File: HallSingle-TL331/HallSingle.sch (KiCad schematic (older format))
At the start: 11 parts, among them J1 Conn_01x03, U1 SS49E, U2 TL331

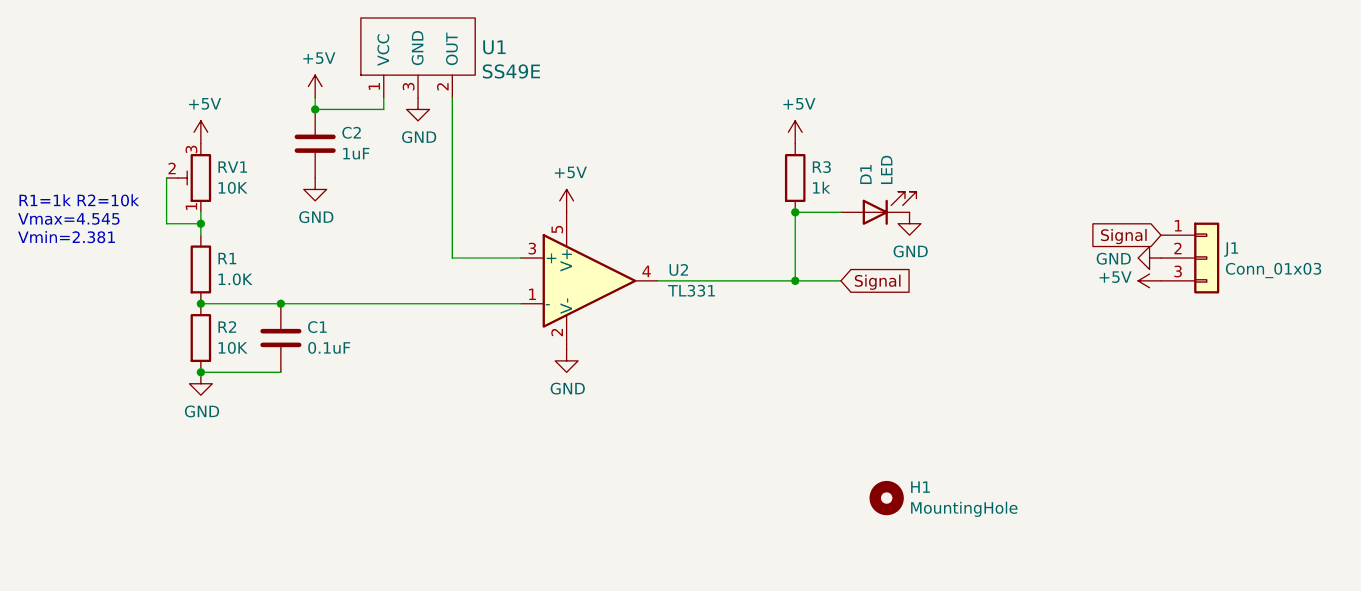
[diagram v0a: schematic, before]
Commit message: Fixed TL orientation. ( previously fixed an error that was not an error ) thining is hard sometimes.
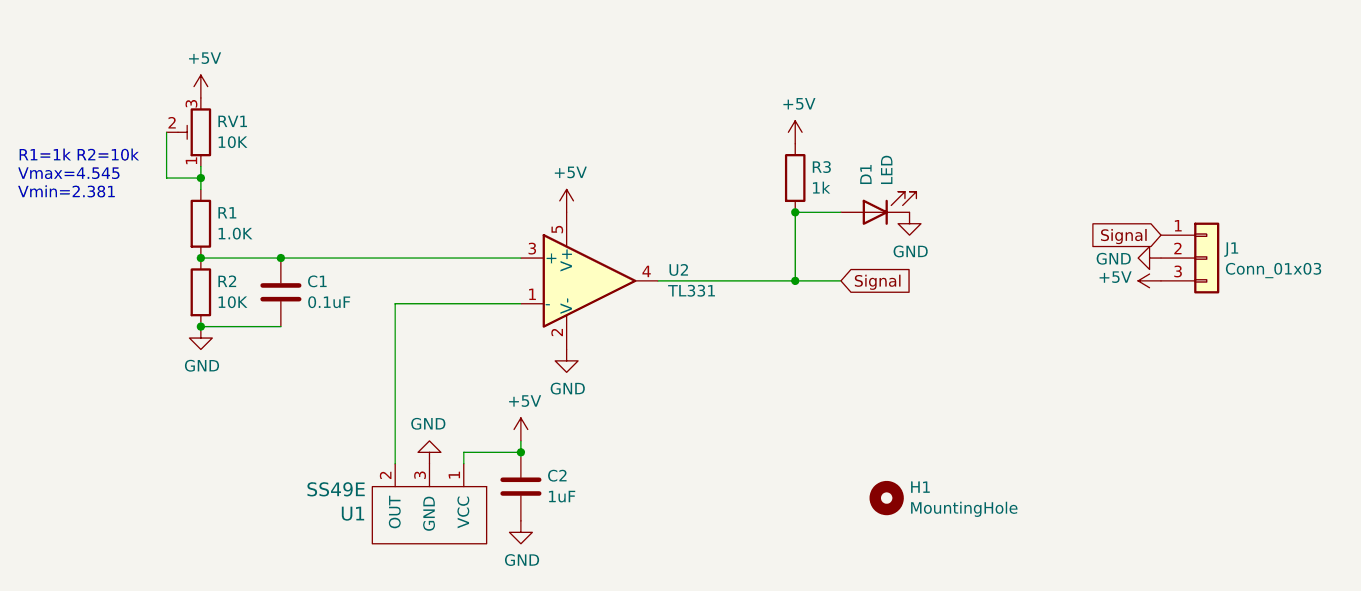
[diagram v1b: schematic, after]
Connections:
- net at U1.2 (OUT): now also U2.1 (-); no longer U2.3 (+)
- net at C1.1, R1.2, R2.1: now also U2.3 (+); no longer U2.1 (-)
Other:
- moved on the sheet: C1, C2, R1, R2, RV1, U1
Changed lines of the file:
@@
 L HallEffect:SS49E U1
 U 1 1 5FEA3EB5
-P 4050 1500
-F 0 "U1" H 4328 1620 60  0000 L CNN
-F 1 "SS49E" H 4328 1514 60  0000 L CNN
-F 2 "HallEffect:SOT-23" H 3950 1500 60  0001 C CNN
-F 3 "" H 3950 1500 60  0001 C CNN
-	1    4050 1500
-	1    0    0    -1
+P 4100 3300
+F 0 "U1" H 4378 3420 60  0000 L CNN
+F 1 "SS49E" H 4378 3314 60  0000 L CNN
+F 2 "HallEffect:SOT-23" H 4000 3300 60  0001 C CNN
+F 3 "" H 4000 3300 60  0001 C CNN
+	1    4100 3300
+	-1   0    0    1
 $EndComp
 $Comp
 L power:GND #PWR05
 U 1 1 5FEA483D
-P 4050 1600
-F 0 "#PWR05" H 4050 1350 50  0001 C CNN
-F 1 "GND" H 4055 1427 50  0000 C CNN
-F 2 "" H 4050 1600 50  0001 C CNN
-F 3 "" H 4050 1600 50  0001 C CNN
-	1    4050 1600
-	1    0    0    -1
+P 4100 3200
+F 0 "#PWR05" H 4100 2950 50  0001 C CNN
+F 1 "GND" H 4105 3027 50  0000 C CNN
+F 2 "" H 4100 3200 50  0001 C CNN
+F 3 "" H 4100 3200 50  0001 C CNN
+	1    4100 3200
+	-1   0    0    1
 $EndComp
 $Comp
 L HallEffect:R R2
 U 1 1 5FEADFC8
-P 3100 2650
-F 0 "R2" H 3170 2696 50  0000 L CNN
-F 1 "10K" H 3170 2605 50  0000 L CNN
-F 2 "HallEffect:R_0805_2012Metric" V 3030 2650 50  0001 C CNN
-F 3 "~" H 3100 2650 50  0001 C CNN
-	1    3100 2650
+P 3100 2450
+F 0 "R2" H 3170 2496 50  0000 L CNN
+F 1 "10K" H 3170 2405 50  0000 L CNN
+F 2 "HallEffect:R_0805_2012Metric" V 3030 2450 50  0001 C CNN
+F 3 "~" H 3100 2450 50  0001 C CNN
+	1    3100 2450
 	1    0    0    -1
 $EndComp
@@
 L HallEffect:R R1
 U 1 1 5FEAE921
-P 3100 2350
-F 0 "R1" H 3170 2396 50  0000 L CNN
-F 1 "1.0K" H 3170 2305 50  0000 L CNN
-F 2 "HallEffect:R_0805_2012Metric" V 3030 2350 50  0001 C CNN
-F 3 "~" H 3100 2350 50  0001 C CNN
-	1    3100 2350
+P 3100 2150
+F 0 "R1" H 3170 2196 50  0000 L CNN
+F 1 "1.0K" H 3170 2105 50  0000 L CNN
+F 2 "HallEffect:R_0805_2012Metric" V 3030 2150 50  0001 C CNN
+F 3 "~" H 3100 2150 50  0001 C CNN
+	1    3100 2150
 	1    0    0    -1
 $EndComp
@@
 L Device:R_POT_TRIM RV1
 U 1 1 5FEAFE4B
-P 3100 1950
-F 0 "RV1" H 3030 1904 50  0000 R CNN
-F 1 "10K" H 3030 1995 50  0000 R CNN
-F 2 "HallEffect:CT6EP103" H 3100 1950 50  0001 C CNN
-F 3 "~" H 3100 1950 50  0001 C CNN
-	1    3100 1950
-	-1   0    0    1
-$EndComp
-Wire Wire Line
-	3100 2500 3450 2500
-Connection ~ 3100 2500
+P 3100 1750
+F 0 "RV1" H 3030 1704 50  0000 R CNN
+F 1 "10K" H 3030 1795 50  0000 R CNN
+F 2 "HallEffect:CT6EP103" H 3100 1750 50  0001 C CNN
+F 3 "~" H 3100 1750 50  0001 C CNN
+	1    3100 1750
+	-1   0    0    1
+$EndComp
+Wire Wire Line
+	3100 2300 3450 2300
+Connection ~ 3100 2300
 $Comp
 L HallEffect:C C1
 U 1 1 5FEB3165
-P 3450 2650
-F 0 "C1" H 3565 2696 50  0000 L CNN
-F 1 "0.1uF" H 3565 2605 50  0000 L CNN
-F 2 "HallEffect:C_0805_2012Metric" H 3488 2500 50  0001 C CNN
-F 3 "~" H 3450 2650 50  0001 C CNN
-	1    3450 2650
-	1    0    0    -1
-$EndComp
-Connection ~ 3450 2500
-Wire Wire Line
-	3450 2500 4500 2500
-Wire Wire Line
-	3450 2800 3100 2800
+P 3450 2450
+F 0 "C1" H 3565 2496 50  0000 L CNN
+F 1 "0.1uF" H 3565 2405 50  0000 L CNN
+F 2 "HallEffect:C_0805_2012Metric" H 3488 2300 50  0001 C CNN
+F 3 "~" H 3450 2450 50  0001 C CNN
+	1    3450 2450
+	1    0    0    -1
+$EndComp
+Connection ~ 3450 2300
+Wire Wire Line
+	3450 2300 4500 2300
+Wire Wire Line
+	3450 2600 3100 2600
 $Comp
 L power:GND #PWR02
 U 1 1 5FEB3CBB
-P 3100 2800
-F 0 "#PWR02" H 3100 2550 50  0001 C CNN
-F 1 "GND" H 3105 2627 50  0000 C CNN
-F 2 "" H 3100 2800 50  0001 C CNN
-F 3 "" H 3100 2800 50  0001 C CNN
-	1    3100 2800
-	1    0    0    -1
-$EndComp
-Connection ~ 3100 2800
+P 3100 2600
+F 0 "#PWR02" H 3100 2350 50  0001 C CNN
+F 1 "GND" H 3105 2427 50  0000 C CNN
+F 2 "" H 3100 2600 50  0001 C CNN
+F 3 "" H 3100 2600 50  0001 C CNN
+	1    3100 2600
+	1    0    0    -1
+$EndComp
+Connection ~ 3100 2600
 $Comp
 L power:+5V #PWR01
 U 1 1 5FEB4703
-P 3100 1800
-F 0 "#PWR01" H 3100 1650 50  0001 C CNN
-F 1 "+5V" H 3115 1973 50  0000 C CNN
-F 2 "" H 3100 1800 50  0001 C CNN
-F 3 "" H 3100 1800 50  0001 C CNN
-	1    3100 1800
+P 3100 1600
+F 0 "#PWR01" H 3100 1450 50  0001 C CNN
+F 1 "+5V" H 3115 1773 50  0000 C CNN
+F 2 "" H 3100 1600 50  0001 C CNN
+F 3 "" H 3100 1600 50  0001 C CNN
+	1    3100 1600
 	1    0    0    -1
 $EndComp
@@
 Text GLabel 5900 2400 2    50   Input ~ 0
 Signal
-Text Notes 2300 2250 0    50   ~ 0
+Text Notes 2300 2050 0    50   ~ 0
 R1=1k R2=10k\nVmax=4.545\nVmin=2.381
 Wire Wire Line
-	3100 2100 3100 2150
-Wire Wire Line
-	2950 1950 2950 2150
-Wire Wire Line
-	2950 2150 3100 2150
-Connection ~ 3100 2150
-Wire Wire Line
-	3100 2150 3100 2200
+	3100 1900 3100 1950
+Wire Wire Line
+	2950 1750 2950 1950
+Wire Wire Line
+	2950 1950 3100 1950
+Connection ~ 3100 1950
+Wire Wire Line
+	3100 1950 3100 2000
 Wire Wire Line
 	5100 2400 5700 2400
@@
 L HallEffect:C C2
 U 1 1 5FEAD587
-P 3600 1800
-F 0 "C2" H 3715 1846 50  0000 L CNN
-F 1 "1uF" H 3715 1755 50  0000 L CNN
-F 2 "HallEffect:C_0805_2012Metric" H 3638 1650 50  0001 C CNN
-F 3 "~" H 3600 1800 50  0001 C CNN
-	1    3600 1800
+P 4500 3300
+F 0 "C2" H 4615 3346 50  0000 L CNN
+F 1 "1uF" H 4615 3255 50  0000 L CNN
+F 2 "HallEffect:C_0805_2012Metric" H 4538 3150 50  0001 C CNN
+F 3 "~" H 4500 3300 50  0001 C CNN
+	1    4500 3300
 	1    0    0    -1
 $EndComp
@@
 L power:GND #PWR04
 U 1 1 5FEA5FC6
-P 3600 1950
-F 0 "#PWR04" H 3600 1700 50  0001 C CNN
-F 1 "GND" H 3605 1777 50  0000 C CNN
-F 2 "" H 3600 1950 50  0001 C CNN
-F 3 "" H 3600 1950 50  0001 C CNN
-	1    3600 1950
+P 4500 3450
+F 0 "#PWR04" H 4500 3200 50  0001 C CNN
+F 1 "GND" H 4505 3277 50  0000 C CNN
+F 2 "" H 4500 3450 50  0001 C CNN
+F 3 "" H 4500 3450 50  0001 C CNN
+	1    4500 3450
 	1    0    0    -1
 $EndComp
@@
 L power:+5V #PWR03
 U 1 1 5FEA5973
-P 3600 1600
-F 0 "#PWR03" H 3600 1450 50  0001 C CNN
-F 1 "+5V" H 3615 1773 50  0000 C CNN
-F 2 "" H 3600 1600 50  0001 C CNN
-F 3 "" H 3600 1600 50  0001 C CNN
-	1    3600 1600
-	1    0    0    -1
-$EndComp
-Wire Wire Line
-	3600 1650 3600 1600
-Wire Wire Line
-	3900 1650 3900 1600
-Wire Wire Line
-	4200 1600 4200 2300
-Wire Wire Line
-	4200 2300 4500 2300
-Wire Wire Line
-	3600 1650 3900 1650
-Connection ~ 3600 1650
+P 4500 3100
+F 0 "#PWR03" H 4500 2950 50  0001 C CNN
+F 1 "+5V" H 4515 3273 50  0000 C CNN
+F 2 "" H 4500 3100 50  0001 C CNN
+F 3 "" H 4500 3100 50  0001 C CNN
+	1    4500 3100
+	1    0    0    -1
+$EndComp
+Wire Wire Line
+	4500 3150 4500 3100
+Wire Wire Line
+	4250 3150 4250 3200
+Wire Wire Line
+	3950 3200 3950 2500
+Wire Wire Line
+	4250 3150 4500 3150
+Connection ~ 4500 3150
+Wire Wire Line
+	3950 2500 4500 2500
 $EndSCHEMATC

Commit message: Tinier components and different LED schematic
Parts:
- C1, C2: footprint HallEffect:C_0805_2012Metric -> Capacitor_SMD:C_0603_1608Metric
- J1: footprint HallEffect:PinHeader_1x03_P2.54mm_Vertical -> Connector_JST:JST_XH_B3B-XH-A_1x03_P2.50mm_Vertical
- R1, R2, R3: footprint HallEffect:R_0805_2012Metric -> Resistor_SMD:R_0603_1608Metric
- RV1: footprint HallEffect:CT6EP103 -> HallEffect:Potentiometer_3x3
- U2: symbol Comparator:TL331 -> HallSingle-rescue:TL331-Comparator
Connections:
- net GND: no longer D1.1 (K)
- net Signal: now also D1.1 (K); no longer D1.2 (A), R3.2
- new net: D1.2 (A), R3.2
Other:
- moved on the sheet: D1, R3
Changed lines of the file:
@@
 F 0 "J1" H 7580 2342 50  0000 L CNN
 F 1 "Conn_01x03" H 7580 2251 50  0000 L CNN
-F 2 "HallEffect:PinHeader_1x03_P2.54mm_Vertical" H 7500 2300 50  0001 C CNN
+F 2 "Connector_JST:JST_XH_B3B-XH-A_1x03_P2.50mm_Vertical" H 7500 2300 50  0001 C CNN
 F 3 "~" H 7500 2300 50  0001 C CNN
 	1    7500 2300
@@
 F 0 "R2" H 3170 2496 50  0000 L CNN
 F 1 "10K" H 3170 2405 50  0000 L CNN
-F 2 "HallEffect:R_0805_2012Metric" V 3030 2450 50  0001 C CNN
+F 2 "Resistor_SMD:R_0603_1608Metric" V 3030 2450 50  0001 C CNN
 F 3 "~" H 3100 2450 50  0001 C CNN
 	1    3100 2450
@@
 F 0 "R1" H 3170 2196 50  0000 L CNN
 F 1 "1.0K" H 3170 2105 50  0000 L CNN
-F 2 "HallEffect:R_0805_2012Metric" V 3030 2150 50  0001 C CNN
+F 2 "Resistor_SMD:R_0603_1608Metric" V 3030 2150 50  0001 C CNN
 F 3 "~" H 3100 2150 50  0001 C CNN
 	1    3100 2150
@@
 F 0 "RV1" H 3030 1704 50  0000 R CNN
 F 1 "10K" H 3030 1795 50  0000 R CNN
-F 2 "HallEffect:CT6EP103" H 3100 1750 50  0001 C CNN
+F 2 "HallEffect:Potentiometer_3x3" H 3100 1750 50  0001 C CNN
 F 3 "~" H 3100 1750 50  0001 C CNN
 	1    3100 1750
@@
 F 0 "C1" H 3565 2496 50  0000 L CNN
 F 1 "0.1uF" H 3565 2405 50  0000 L CNN
-F 2 "HallEffect:C_0805_2012Metric" H 3488 2300 50  0001 C CNN
+F 2 "Capacitor_SMD:C_0603_1608Metric" H 3488 2300 50  0001 C CNN
 F 3 "~" H 3450 2450 50  0001 C CNN
 	1    3450 2450
@@
 L HallEffect:R R3
 U 1 1 5FEB5185
-P 5700 1950
-F 0 "R3" H 5770 1996 50  0000 L CNN
-F 1 "1k" H 5770 1905 50  0000 L CNN
-F 2 "HallEffect:R_0805_2012Metric" V 5630 1950 50  0001 C CNN
-F 3 "~" H 5700 1950 50  0001 C CNN
-	1    5700 1950
+P 5550 1700
+F 0 "R3" H 5620 1746 50  0000 L CNN
+F 1 "1k" H 5620 1655 50  0000 L CNN
+F 2 "Resistor_SMD:R_0603_1608Metric" V 5480 1700 50  0001 C CNN
+F 3 "~" H 5550 1700 50  0001 C CNN
+	1    5550 1700
 	1    0    0    -1
 $EndComp
@@
 L Device:LED D1
 U 1 1 5FEB5CD2
-P 6050 2100
-F 0 "D1" V 6089 1983 50  0000 R CNN
-F 1 "LED" V 5998 1983 50  0000 R CNN
-F 2 "HallEffect:LED_0805_2012Metric" H 6050 2100 50  0001 C CNN
-F 3 "~" H 6050 2100 50  0001 C CNN
-	1    6050 2100
-	-1   0    0    1
+P 5550 2050
+F 0 "D1" V 5589 1933 50  0000 R CNN
+F 1 "LED" V 5498 1933 50  0000 R CNN
+F 2 "HallEffect:LED_0805_2012Metric" H 5550 2050 50  0001 C CNN
+F 3 "~" H 5550 2050 50  0001 C CNN
+	1    5550 2050
+	0    -1   -1   0
 $EndComp
 $Comp
 L power:+5V #PWR08
 U 1 1 5FEB6CEE
-P 5700 1800
-F 0 "#PWR08" H 5700 1650 50  0001 C CNN
-F 1 "+5V" H 5715 1973 50  0000 C CNN
-F 2 "" H 5700 1800 50  0001 C CNN
-F 3 "" H 5700 1800 50  0001 C CNN
-	1    5700 1800
+P 5550 1550
+F 0 "#PWR08" H 5550 1400 50  0001 C CNN
+F 1 "+5V" H 5565 1723 50  0000 C CNN
+F 2 "" H 5550 1550 50  0001 C CNN
+F 3 "" H 5550 1550 50  0001 C CNN
+	1    5550 1550
 	1    0    0    -1
 $EndComp
@@
 	3100 1950 3100 2000
 Wire Wire Line
-	5100 2400 5700 2400
-$Comp
-L power:GND #PWR011
-U 1 1 6007DD31
-P 6200 2100
-F 0 "#PWR011" H 6200 1850 50  0001 C CNN
-F 1 "GND" H 6205 1927 50  0000 C CNN
-F 2 "" H 6200 2100 50  0001 C CNN
-F 3 "" H 6200 2100 50  0001 C CNN
-	1    6200 2100
-	1    0    0    -1
-$EndComp
-Wire Wire Line
-	5900 2100 5700 2100
-Wire Wire Line
-	5700 2100 5700 2400
-Connection ~ 5700 2100
-Connection ~ 5700 2400
-Wire Wire Line
-	5700 2400 5900 2400
+	5550 1850 5550 1900
 $Comp
 L HallEffect:MountingHole H1
@@
 $EndComp
 $Comp
-L Comparator:TL331 U2
+L HallSingle-rescue:TL331-Comparator U2
 U 1 1 6007B14C
 P 4800 2400
@@
 F 0 "C2" H 4615 3346 50  0000 L CNN
 F 1 "1uF" H 4615 3255 50  0000 L CNN
-F 2 "HallEffect:C_0805_2012Metric" H 4538 3150 50  0001 C CNN
+F 2 "Capacitor_SMD:C_0603_1608Metric" H 4538 3150 50  0001 C CNN
 F 3 "~" H 4500 3300 50  0001 C CNN
 	1    4500 3300
@@
 Wire Wire Line
 	3950 2500 4500 2500
+Wire Wire Line
+	5100 2400 5550 2400
+Wire Wire Line
+	5550 2200 5550 2400
+Connection ~ 5550 2400
+Wire Wire Line
+	5550 2400 5900 2400
 $EndSCHEMATC

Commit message: Back to 0805 because it fits
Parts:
- C1, C2: footprint Capacitor_SMD:C_0603_1608Metric -> Capacitor_SMD:C_0805_2012Metric
- R1, R2, R3: footprint Resistor_SMD:R_0603_1608Metric -> Resistor_SMD:R_0805_2012Metric
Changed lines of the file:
@@
 F 0 "R2" H 3170 2496 50  0000 L CNN
 F 1 "10K" H 3170 2405 50  0000 L CNN
-F 2 "Resistor_SMD:R_0603_1608Metric" V 3030 2450 50  0001 C CNN
+F 2 "Resistor_SMD:R_0805_2012Metric" V 3030 2450 50  0001 C CNN
 F 3 "~" H 3100 2450 50  0001 C CNN
 	1    3100 2450
@@
 F 0 "R1" H 3170 2196 50  0000 L CNN
 F 1 "1.0K" H 3170 2105 50  0000 L CNN
-F 2 "Resistor_SMD:R_0603_1608Metric" V 3030 2150 50  0001 C CNN
+F 2 "Resistor_SMD:R_0805_2012Metric" V 3030 2150 50  0001 C CNN
 F 3 "~" H 3100 2150 50  0001 C CNN
 	1    3100 2150
@@
 F 0 "C1" H 3565 2496 50  0000 L CNN
 F 1 "0.1uF" H 3565 2405 50  0000 L CNN
-F 2 "Capacitor_SMD:C_0603_1608Metric" H 3488 2300 50  0001 C CNN
+F 2 "Capacitor_SMD:C_0805_2012Metric" H 3488 2300 50  0001 C CNN
 F 3 "~" H 3450 2450 50  0001 C CNN
 	1    3450 2450
@@
 F 0 "R3" H 5620 1746 50  0000 L CNN
 F 1 "1k" H 5620 1655 50  0000 L CNN
-F 2 "Resistor_SMD:R_0603_1608Metric" V 5480 1700 50  0001 C CNN
+F 2 "Resistor_SMD:R_0805_2012Metric" V 5480 1700 50  0001 C CNN
 F 3 "~" H 5550 1700 50  0001 C CNN
 	1    5550 1700
@@
 F 0 "C2" H 4615 3346 50  0000 L CNN
 F 1 "1uF" H 4615 3255 50  0000 L CNN
-F 2 "Capacitor_SMD:C_0603_1608Metric" H 4538 3150 50  0001 C CNN
+F 2 "Capacitor_SMD:C_0805_2012Metric" H 4538 3150 50  0001 C CNN
 F 3 "~" H 4500 3300 50  0001 C CNN
 	1    4500 3300
